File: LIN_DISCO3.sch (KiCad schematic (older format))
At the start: 20 parts, among them J1 Conn_01x06_Female, U1 PIC16F628-xxISO, U2 MCP1804x-5002xMB, U3 Si9243A

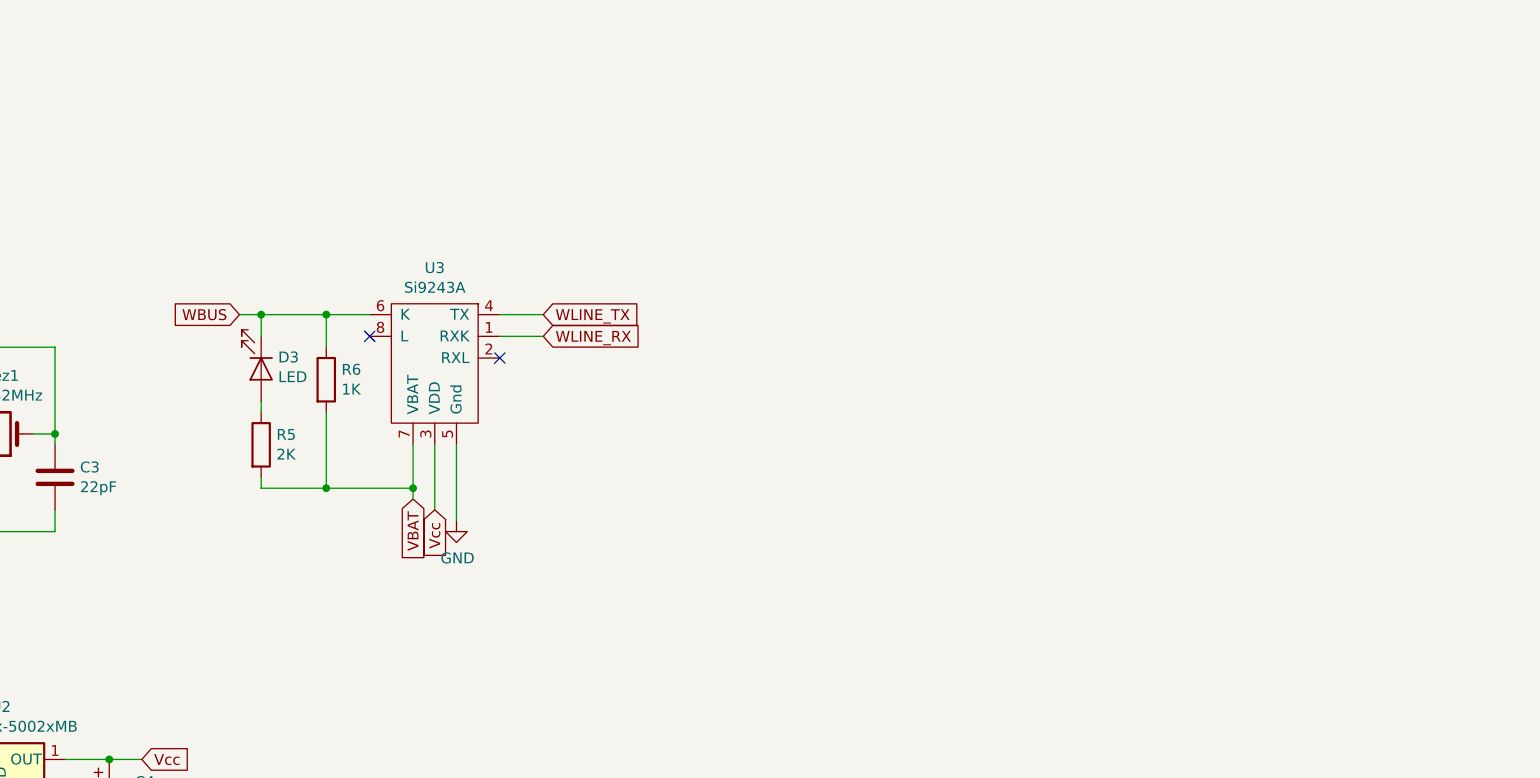
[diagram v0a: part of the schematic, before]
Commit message: transceiver changed to transistor cascade
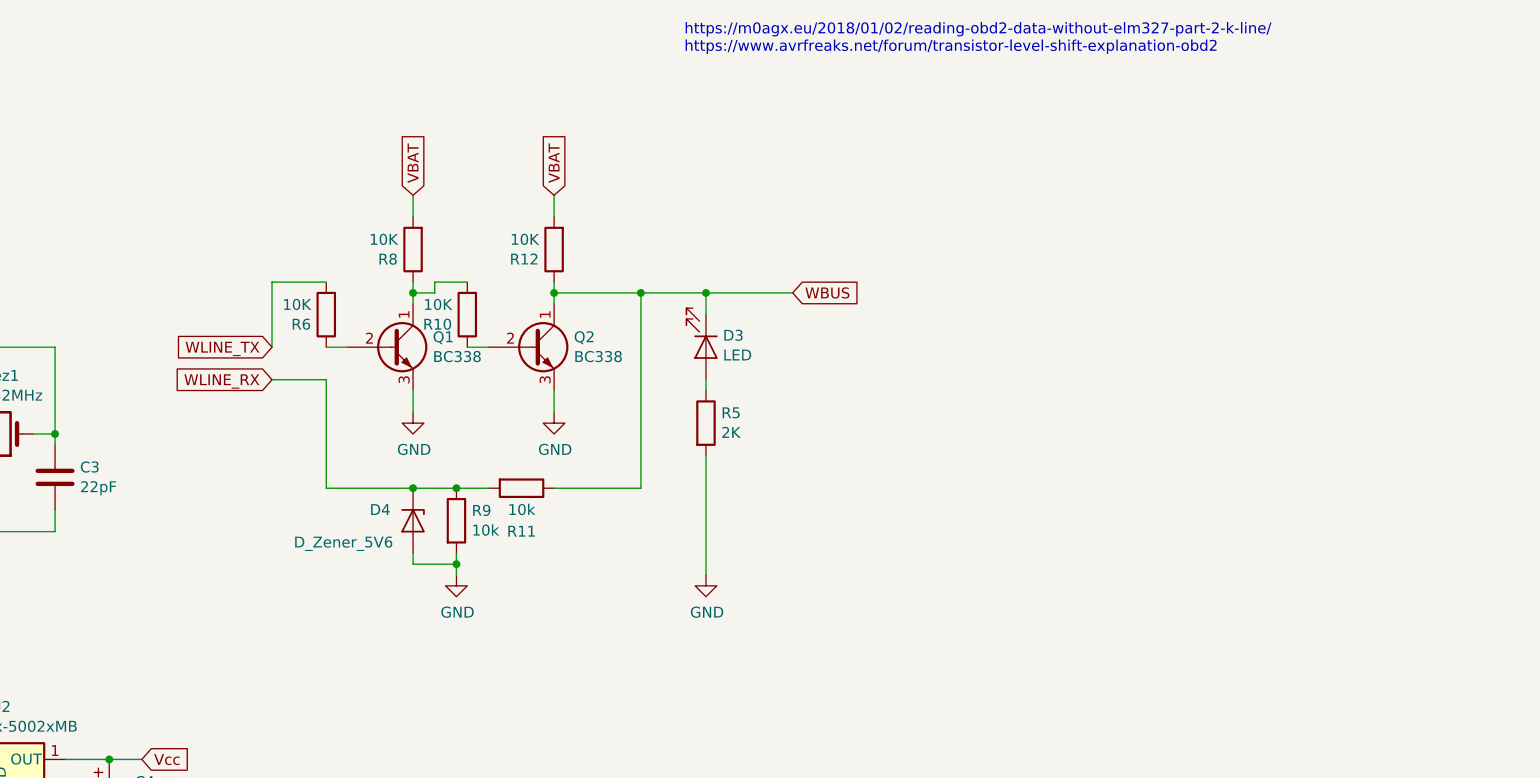
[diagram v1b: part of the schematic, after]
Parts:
- removed U3: Si9243A, Package_SO:SOIC-8_3.9x4.9mm_P1.27mm, symbol vishay_Si9243A:Si9243A
- added D4: D_Zener_5V6, Diode_SMD:D_0805_2012Metric_Pad1.15x1.40mm_HandSolder, symbol Device:D_Zener
- added Q1, Q2: BC338, Package_TO_SOT_THT:TO-92_Inline, symbol Transistor_BJT:BC338
- added R10, R12, R8: 10K, Resistor_SMD:R_0805_2012Metric_Pad1.15x1.40mm_HandSolder, symbol Device:R
- added R11, R9: 10k, Resistor_SMD:R_0805_2012Metric_Pad1.15x1.40mm_HandSolder, symbol Device:R
- R6: value 1K -> 10K
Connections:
- net GND: now also R5.2, D4.2 (A), Q1.3 (E), Q2.3 (E), R9.2
- net VBAT: now also R12.2, R8.2; no longer R5.2, R6.2
- net WBUS: now also Q2.1 (C), R11.1, R12.1; no longer R6.1
- net WLINE_RX: now also D4.1 (K), R11.2, R9.1
- net WLINE_TX: now also R6.2
- new net: Q1.1 (C), R10.2, R8.1
- new net: Q1.2 (B), R6.1
- new net: Q2.2 (B), R10.1
- no-connect marks 9 -> 7
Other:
- note added: "https://m0agx.eu/2018/01/02/reading-obd2-data-without-elm327-part-2-k-line/\nhttps://www.avrfreaks.net/forum/transistor-level-shift-explanation-obd2"
- moved on the sheet: D3, R5

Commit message: diodes and transistors case changed
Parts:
- removed Q1, Q2: BC338, Package_TO_SOT_THT:TO-92_Inline, symbol Transistor_BJT:BC338
- added Q1, Q2: BC847, Package_TO_SOT_SMD:SOT-23, symbol Transistor_BJT:BC847
- D1, D4: footprint Diode_SMD:D_0805_2012Metric_Pad1.15x1.40mm_HandSolder -> Diode_SMD:D_MiniMELF_Handsoldering
- D2: footprint Diode_SMD:D_0805_2012Metric_Pad1.15x1.40mm_HandSolder -> Diode_SMD:D_2512_6332Metric_Castellated
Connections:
- net GND: now also Q1.2 (E), Q2.2 (E)
- net WBUS: now also Q2.3 (C)
- net at R10.2, R8.1: now also Q1.3 (C)
- net at R6.1: now also Q1.1 (B)
- net at R10.1: now also Q2.1 (B)
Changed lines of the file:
@@
 F 0 "D2" V 5196 5221 50  0000 R CNN
 F 1 "D_Zener_5V6" V 5105 5221 50  0000 R CNN
-F 2 "Diode_SMD:D_0805_2012Metric_Pad1.15x1.40mm_HandSolder" H 5150 5300 50  0001 C CNN
+F 2 "Diode_SMD:D_2512_6332Metric_Castellated" H 5150 5300 50  0001 C CNN
 F 3 "~" H 5150 5300 50  0001 C CNN
 	1    5150 5300
@@
 F 0 "D1" V 4854 5779 50  0000 L CNN
 F 1 "D_Zener_5V6" V 4945 5779 50  0000 L CNN
-F 2 "Diode_SMD:D_0805_2012Metric_Pad1.15x1.40mm_HandSolder" H 4900 5700 50  0001 C CNN
+F 2 "Diode_SMD:D_MiniMELF_Handsoldering" H 4900 5700 50  0001 C CNN
 F 3 "~" H 4900 5700 50  0001 C CNN
 	1    4900 5700
@@
 https://m0agx.eu/2018/01/02/reading-obd2-data-without-elm327-part-2-k-line/\nhttps://www.avrfreaks.net/forum/transistor-level-shift-explanation-obd2
 $Comp
-L Transistor_BJT:BC338 Q1
-U 1 1 620921E1
-P 6400 2100
-F 0 "Q1" H 6591 2146 50  0000 L CNN
-F 1 "BC338" H 6591 2055 50  0000 L CNN
-F 2 "Package_TO_SOT_THT:TO-92_Inline" H 6600 2025 50  0001 L CIN
-F 3 "http://diotec.com/tl_files/diotec/files/pdf/datasheets/bc337" H 6400 2100 50  0001 L CNN
-	1    6400 2100
-	1    0    0    -1
-$EndComp
-$Comp
 L Device:R R6
 U 1 1 62093D29
@@
 $EndComp
 $Comp
-L Transistor_BJT:BC338 Q2
-U 1 1 620B23DD
-P 7050 2100
-F 0 "Q2" H 7241 2146 50  0000 L CNN
-F 1 "BC338" H 7241 2055 50  0000 L CNN
-F 2 "Package_TO_SOT_THT:TO-92_Inline" H 7250 2025 50  0001 L CIN
-F 3 "http://diotec.com/tl_files/diotec/files/pdf/datasheets/bc337" H 7050 2100 50  0001 L CNN
-	1    7050 2100
-	1    0    0    -1
-$EndComp
-$Comp
 L Device:R R10
 U 1 1 620B23E7
@@
 F 0 "D4" V 6450 2700 50  0000 L CNN
 F 1 "D_Zener_5V6" V 6600 2350 50  0000 L CNN
-F 2 "Diode_SMD:D_0805_2012Metric_Pad1.15x1.40mm_HandSolder" H 6500 2900 50  0001 C CNN
+F 2 "Diode_SMD:D_MiniMELF_Handsoldering" H 6500 2900 50  0001 C CNN
 F 3 "~" H 6500 2900 50  0001 C CNN
 	1    6500 2900
@@
 	1    0    0    -1
 $EndComp
+$Comp
+L Transistor_BJT:BC847 Q1
+U 1 1 620C022A
+P 6400 2100
+F 0 "Q1" H 6591 2146 50  0000 L CNN
+F 1 "BC847" H 6591 2055 50  0000 L CNN
+F 2 "Package_TO_SOT_SMD:SOT-23" H 6600 2025 50  0001 L CIN
+F 3 "http://www.infineon.com/dgdl/Infineon-BC847SERIES_BC848SERIES_BC849SERIES_BC850SERIES-DS-v01_01-en.pdf?fileId=db3a304314dca389011541d4630a1657" H 6400 2100 50  0001 L CNN
+	1    6400 2100
+	1    0    0    -1
+$EndComp
+$Comp
+L Transistor_BJT:BC847 Q2
+U 1 1 620C0B3E
+P 7050 2100
+F 0 "Q2" H 7241 2146 50  0000 L CNN
+F 1 "BC847" H 7241 2055 50  0000 L CNN
+F 2 "Package_TO_SOT_SMD:SOT-23" H 7250 2025 50  0001 L CIN
+F 3 "http://www.infineon.com/dgdl/Infineon-BC847SERIES_BC848SERIES_BC849SERIES_BC850SERIES-DS-v01_01-en.pdf?fileId=db3a304314dca389011541d4630a1657" H 7050 2100 50  0001 L CNN
+	1    7050 2100
+	1    0    0    -1
+$EndComp

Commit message: updated board for sot23 and miniMELF
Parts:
- added D5: LED, LED_SMD:LED_0805_2012Metric_Pad1.15x1.40mm_HandSolder, symbol Device:LED
- added R13: 2K, Resistor_SMD:R_0805_2012Metric_Pad1.15x1.40mm_HandSolder, symbol Device:R
- D1, D4: footprint Diode_SMD:D_MiniMELF_Handsoldering -> Diode_SMD:D_MiniMELF
- D2: footprint Diode_SMD:D_2512_6332Metric_Castellated -> Diode_SMD:D_MiniMELF
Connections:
- net GND: now also R13.2
- net W_ACTIVE: now reaches U1.17 (AN0/RA0)
- net W_ACTIVE: now also D5.2 (A)
- new net: D5.1 (K), R13.1
- no-connect marks 7 -> 6
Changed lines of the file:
@@
 Text GLabel 8250 1850 2    50   Input ~ 0
 WBUS
-NoConn ~ 3700 1800
 NoConn ~ 3700 1900
 NoConn ~ 3700 2000
@@
 F 0 "D2" V 5196 5221 50  0000 R CNN
 F 1 "D_Zener_5V6" V 5105 5221 50  0000 R CNN
-F 2 "Diode_SMD:D_2512_6332Metric_Castellated" H 5150 5300 50  0001 C CNN
+F 2 "Diode_SMD:D_MiniMELF" H 5150 5300 50  0001 C CNN
 F 3 "~" H 5150 5300 50  0001 C CNN
 	1    5150 5300
@@
 F 0 "D1" V 4854 5779 50  0000 L CNN
 F 1 "D_Zener_5V6" V 4945 5779 50  0000 L CNN
-F 2 "Diode_SMD:D_MiniMELF_Handsoldering" H 4900 5700 50  0001 C CNN
+F 2 "Diode_SMD:D_MiniMELF" H 4900 5700 50  0001 C CNN
 F 3 "~" H 4900 5700 50  0001 C CNN
 	1    4900 5700
@@
 F 0 "D4" V 6450 2700 50  0000 L CNN
 F 1 "D_Zener_5V6" V 6600 2350 50  0000 L CNN
-F 2 "Diode_SMD:D_MiniMELF_Handsoldering" H 6500 2900 50  0001 C CNN
+F 2 "Diode_SMD:D_MiniMELF" H 6500 2900 50  0001 C CNN
 F 3 "~" H 6500 2900 50  0001 C CNN
 	1    6500 2900
@@
 	1    0    0    -1
 $EndComp
+Text GLabel 3800 1800 2    50   Input ~ 0
+W_ACTIVE
+Wire Wire Line
+	3700 1800 3800 1800
+Text GLabel 6450 5450 0    50   Input ~ 0
+W_ACTIVE
+$Comp
+L Device:LED D5
+U 1 1 620E162E
+P 6600 5700
+F 0 "D5" V 6547 5778 50  0000 L CNN
+F 1 "LED" V 6638 5778 50  0000 L CNN
+F 2 "LED_SMD:LED_0805_2012Metric_Pad1.15x1.40mm_HandSolder" H 6600 5700 50  0001 C CNN
+F 3 "~" H 6600 5700 50  0001 C CNN
+	1    6600 5700
+	0    -1   -1   0
+$EndComp
+Wire Wire Line
+	6600 5550 6600 5450
+Wire Wire Line
+	6600 5850 6600 5900
+$Comp
+L power:GND #PWR0112
+U 1 1 620E163A
+P 6600 6300
+F 0 "#PWR0112" H 6600 6050 50  0001 C CNN
+F 1 "GND" H 6605 6127 50  0000 C CNN
+F 2 "" H 6600 6300 50  0001 C CNN
+F 3 "" H 6600 6300 50  0001 C CNN
+	1    6600 6300
+	1    0    0    -1
+$EndComp
+Wire Wire Line
+	6600 6200 6600 6300
+$Comp
+L Device:R R13
+U 1 1 620E1645
+P 6600 6050
+F 0 "R13" H 6670 6096 50  0000 L CNN
+F 1 "2K" H 6670 6005 50  0000 L CNN
+F 2 "Resistor_SMD:R_0805_2012Metric_Pad1.15x1.40mm_HandSolder" V 6530 6050 50  0001 C CNN
+F 3 "~" H 6600 6050 50  0001 C CNN
+	1    6600 6050
+	1    0    0    -1
+$EndComp
+Wire Wire Line
+	6450 5450 6600 5450
 $EndSCHEMATC

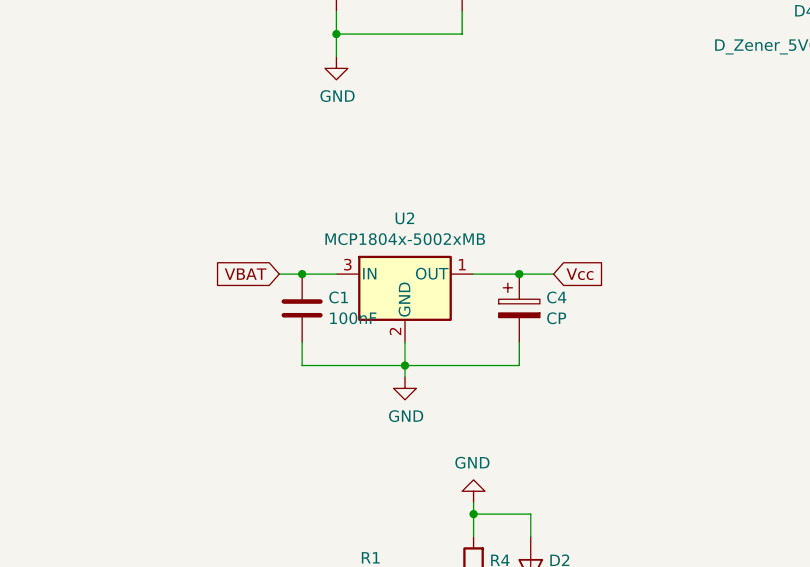
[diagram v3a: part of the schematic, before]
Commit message: board layout prepared for production
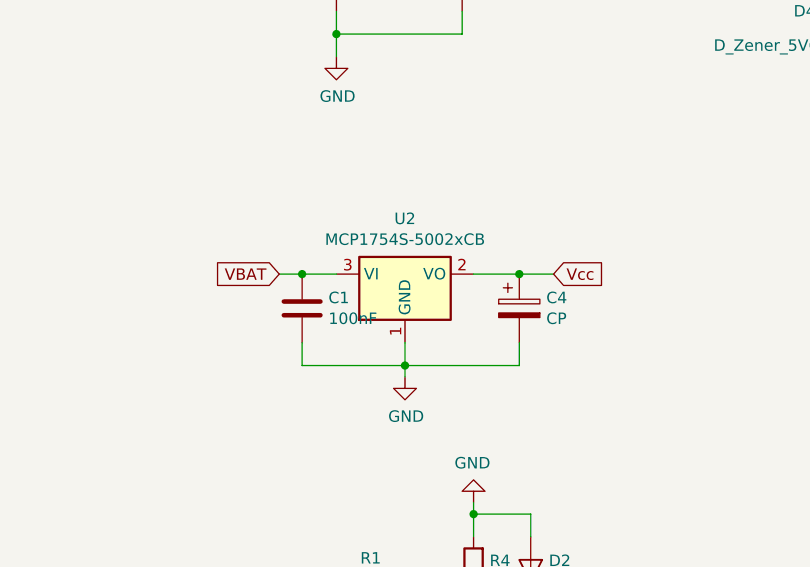
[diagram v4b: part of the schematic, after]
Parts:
- removed U2: MCP1804x-5002xMB, Package_TO_SOT_SMD:SOT-89-3, symbol Regulator_Linear:MCP1804x-5002xMB
- added U2: MCP1754S-5002xCB, Package_TO_SOT_SMD:SOT-223, symbol Regulator_Linear:MCP1754S-5002xCB
- Rez1: footprint Crystal:Crystal_SMD_0603-2Pin_6.0x3.5mm_HandSoldering -> Crystal:Crystal_HC49-U_Vertical
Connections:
- net GND: now also U2.1 (GND)
- net VBAT: now also U2.3 (VI)
- net Vcc: now also U2.2 (VO)
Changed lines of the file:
@@
 F 0 "Rez1" H 4600 2232 50  0000 C CNN
 F 1 "18.432MHz" H 4600 2323 50  0000 C CNN
-F 2 "Crystal:Crystal_SMD_0603-2Pin_6.0x3.5mm_HandSoldering" H 4600 2500 50  0001 C CNN
+F 2 "Crystal:Crystal_HC49-U_Vertical" H 4600 2500 50  0001 C CNN
 F 3 "~" H 4600 2500 50  0001 C CNN
 	1    4600 2500
@@
 	4000 5550 4300 5550
 $Comp
-L Regulator_Linear:MCP1804x-5002xMB U2
-U 1 1 61F18390
-P 4600 4000
-F 0 "U2" H 4600 4242 50  0000 C CNN
-F 1 "MCP1804x-5002xMB" H 4600 4151 50  0000 C CNN
-F 2 "Package_TO_SOT_SMD:SOT-89-3" H 4600 4200 50  0001 C CIN
-F 3 "http://ww1.microchip.com/downloads/en/DeviceDoc/20002200D.pdf" H 4600 3950 50  0001 C CNN
-	1    4600 4000
-	1    0    0    -1
-$EndComp
-$Comp
 L power:GND #PWR0106
 U 1 1 61F18E84
@@
 Wire Wire Line
 	6450 5450 6600 5450
+$Comp
+L Regulator_Linear:MCP1754S-5002xCB U2
+U 1 1 620C41C7
+P 4600 4000
+F 0 "U2" H 4600 4242 50  0000 C CNN
+F 1 "MCP1754S-5002xCB" H 4600 4151 50  0000 C CNN
+F 2 "Package_TO_SOT_SMD:SOT-223" H 4600 4225 50  0001 C CNN
+F 3 "http://ww1.microchip.com/downloads/en/DeviceDoc/20002276C.pdf" H 4600 4000 50  0001 C CNN
+	1    4600 4000
+	1    0    0    -1
+$EndComp
 $EndSCHEMATC
